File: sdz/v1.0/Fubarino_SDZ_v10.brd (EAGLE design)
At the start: 71.2 x 25.5 mm, 40 parts, among them IC1 PIC32MZXXXXECX064TQFP-10X10, IC2 MCP1702T-3302E/MB, IC3 DSC1033_MICREL_OSCILLATOR3.2X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, J1 MICRO_SD_CARD_SOCKET, J2 M28USEPIN1, J3 M28NOPIN1, J4 MICRO-USB-5P-340015001, J5 MICRO-SDCARD-CONNECTOR-330006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, Q2 32.768 KHz

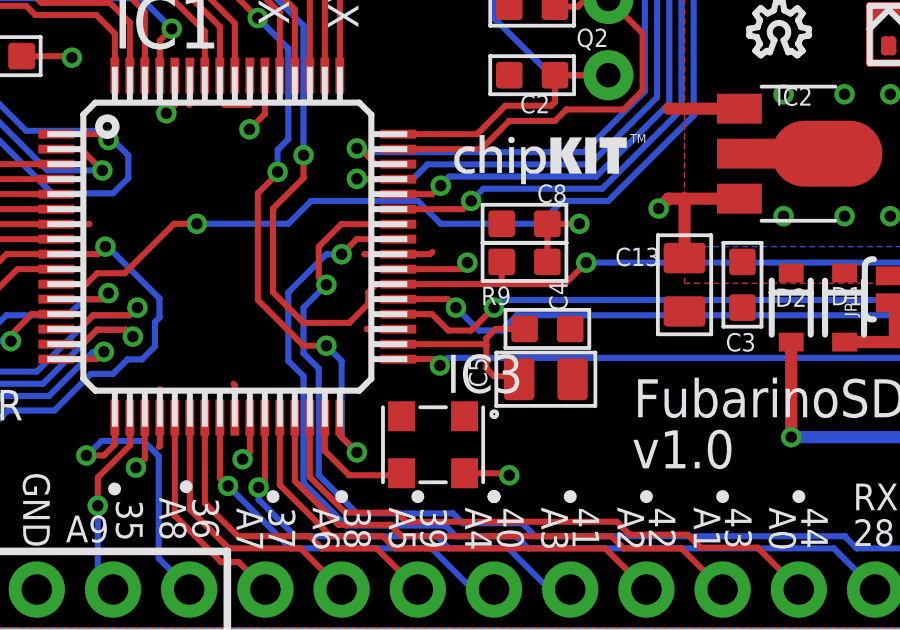
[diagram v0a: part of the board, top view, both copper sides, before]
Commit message: Ooooops. Bad footprint for CPU. Got boards back and they had solder mask on all pins. Updated to new footprint, found D-/D+ swap bug, and send out for new boards.
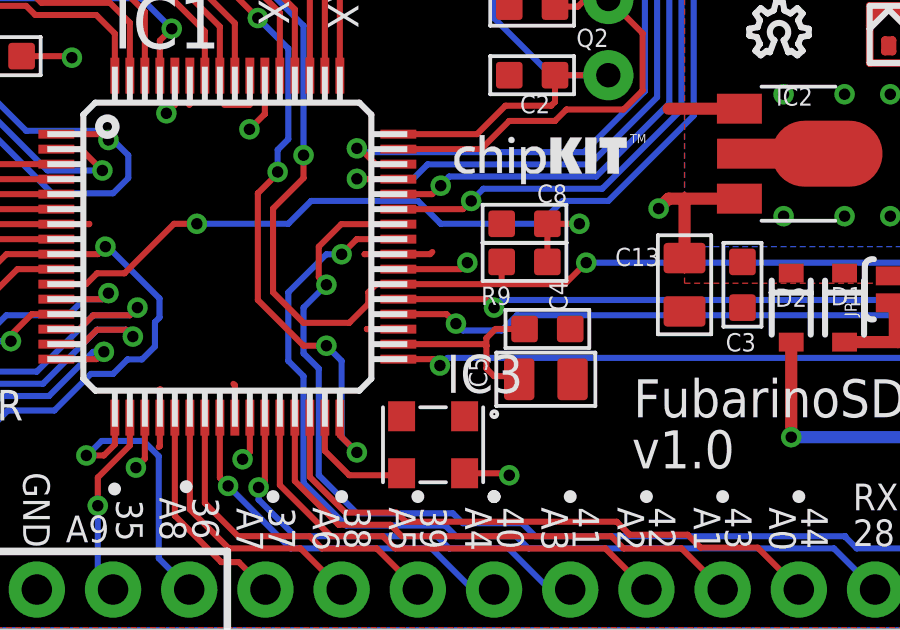
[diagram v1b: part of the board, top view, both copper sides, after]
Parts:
- IC1: value PIC32MZXXXXECX064TQFP-10X10 -> PIC32MZXXXXECX064; device SchmalzHaus:TQFP64-10X10-SOLDERDAMS -> SchmalzHaus:TQFP64-10X10
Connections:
- net D+: now also IC1.37; no longer IC1.36
- net D-: now also IC1.36; no longer IC1.37
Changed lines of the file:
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@@
 <?xml version="1.0" encoding="utf-8"?>
 <!DOCTYPE eagle SYSTEM "eagle.dtd">
-<eagle version="6.4">
+<eagle version="6.5.0">
 <drawing>
 <settings>
@@
 <setting verticaltext="up"/>
 </settings>
-<grid distance="50" unitdist="mil" unit="mil" style="lines" multiple="1" display="yes" altdistance="0.001" altunitdist="inch" altunit="inch"/>
+<grid distance="50" unitdist="mil" unit="inch" style="lines" multiple="1" display="yes" altdistance="0.001" altunitdist="inch" altunit="inch"/>
 <layers>
 <layer number="1" name="Top" color="4" fill="1" visible="yes" active="yes"/>
@@
 <element name="U$4" library="SchmalzHausPublic" package="CHIPKIT_2MM" value="CHIPKIT2MM" x="45.5422" y="14.7066"/>
 <element name="U$5" library="SchmalzHausPublic" package="CHIPKIT_2MM" value="CHIPKIT2MM" x="39.37" y="15.24" rot="MR0"/>
-<element name="IC1" library="SchmalzHaus" package="TQFP64-10X10-SOLDERDAMS" value="PIC32MZXXXXECX064TQFP-10X10" x="38.1" y="12.7"/>
+<element name="IC1" library="SchmalzHaus" package="TQFP64-10X10" value="PIC32MZXXXXECX064" x="38.1" y="12.7"/>
 <element name="D3" library="OPL Eagle Library" package="LED0603" value="GREEN" x="26.67" y="16.51"/>
 <element name="D4" library="OPL Eagle Library" package="LED0603" value="RED" x="26.67" y="7.4422"/>
@@
 </signal>
 <signal name="D+">
-<contactref element="IC1" pad="36"/>
+<contactref element="IC1" pad="37"/>
 <contactref element="J4" pad="3"/>
-<wire x1="43.8" y1="10.45" x2="44.922" y2="10.45" width="0.2032" layer="1"/>
 <via x="46.99" y="10.668" extent="1-16" drill="0.381"/>
 <wire x1="61.976" y1="10.922" x2="63.5" y2="12.446" width="0.2032" layer="16"/>
-<wire x1="44.922" y1="10.45" x2="45.466" y2="9.906" width="0.2032" layer="1"/>
-<wire x1="45.466" y1="9.906" x2="46.228" y2="9.906" width="0.2032" layer="1"/>
-<wire x1="46.228" y1="9.906" x2="46.99" y2="10.668" width="0.2032" layer="1"/>
 <wire x1="46.99" y1="10.668" x2="47.244" y2="10.922" width="0.2032" layer="16"/>
 <wire x1="47.244" y1="10.922" x2="61.976" y2="10.922" width="0.2032" layer="16"/>
@@
 <wire x1="64.008" y1="12.954" x2="63.5" y2="12.446" width="0.2032" layer="1"/>
 <via x="63.5" y="12.446" extent="1-16" drill="0.381"/>
+<wire x1="43.8" y1="10.95" x2="46.708" y2="10.95" width="0.2032" layer="1"/>
+<wire x1="46.708" y1="10.95" x2="46.99" y2="10.668" width="0.2032" layer="1"/>
 </signal>
 <signal name="D-">
-<contactref element="IC1" pad="37"/>
+<contactref element="IC1" pad="36"/>
 <contactref element="J4" pad="2"/>
-<wire x1="43.8" y1="10.95" x2="45.438" y2="10.95" width="0.2032" layer="1"/>
-<via x="45.72" y="10.668" extent="1-16" drill="0.381"/>
+<via x="45.72" y="10.1346" extent="1-16" drill="0.381"/>
 <wire x1="62.738" y1="10.414" x2="63.5" y2="11.176" width="0.2032" layer="16"/>
 <wire x1="63.5" y1="11.176" x2="63.5" y2="11.43" width="0.2032" layer="16"/>
@@
 <wire x1="63.754" y1="11.684" x2="64.008" y2="11.684" width="0.2032" layer="16"/>
 <wire x1="64.008" y1="11.684" x2="64.516" y2="12.192" width="0.2032" layer="16"/>
-<wire x1="45.438" y1="10.95" x2="45.72" y2="10.668" width="0.2032" layer="1"/>
-<wire x1="45.72" y1="10.668" x2="46.482" y2="9.906" width="0.2032" layer="16"/>
-<wire x1="46.482" y1="9.906" x2="47.244" y2="9.906" width="0.2032" layer="16"/>
+<wire x1="45.72" y1="10.1346" x2="45.9486" y2="9.906" width="0.2032" layer="16"/>
+<wire x1="45.9486" y1="9.906" x2="47.244" y2="9.906" width="0.2032" layer="16"/>
 <wire x1="47.244" y1="9.906" x2="47.752" y2="10.414" width="0.2032" layer="16"/>
 <wire x1="47.752" y1="10.414" x2="62.738" y2="10.414" width="0.2032" layer="16"/>
@@
 <wire x1="64.6326" y1="12.0754" x2="64.516" y2="12.192" width="0.2032" layer="1"/>
 <via x="64.516" y="12.192" extent="1-16" drill="0.381"/>
+<wire x1="43.8" y1="10.45" x2="45.4046" y2="10.45" width="0.2032" layer="1"/>
+<wire x1="45.4046" y1="10.45" x2="45.72" y2="10.1346" width="0.2032" layer="1"/>
 </signal>
 <signal name="VBUS">
